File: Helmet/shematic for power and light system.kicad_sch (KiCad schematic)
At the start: 10 parts, among them Q1 IRLZ44N, SW1 SW_DIP_x01, U1 LM340K-5.0/NOPB, U2 LP2950-3.3_TO252, U3 ESP32-WROOM-32, U4 LM340K-5.0/NOPB, U5 ESP32-WROOM-32, U6 LP2950-3.3_TO252

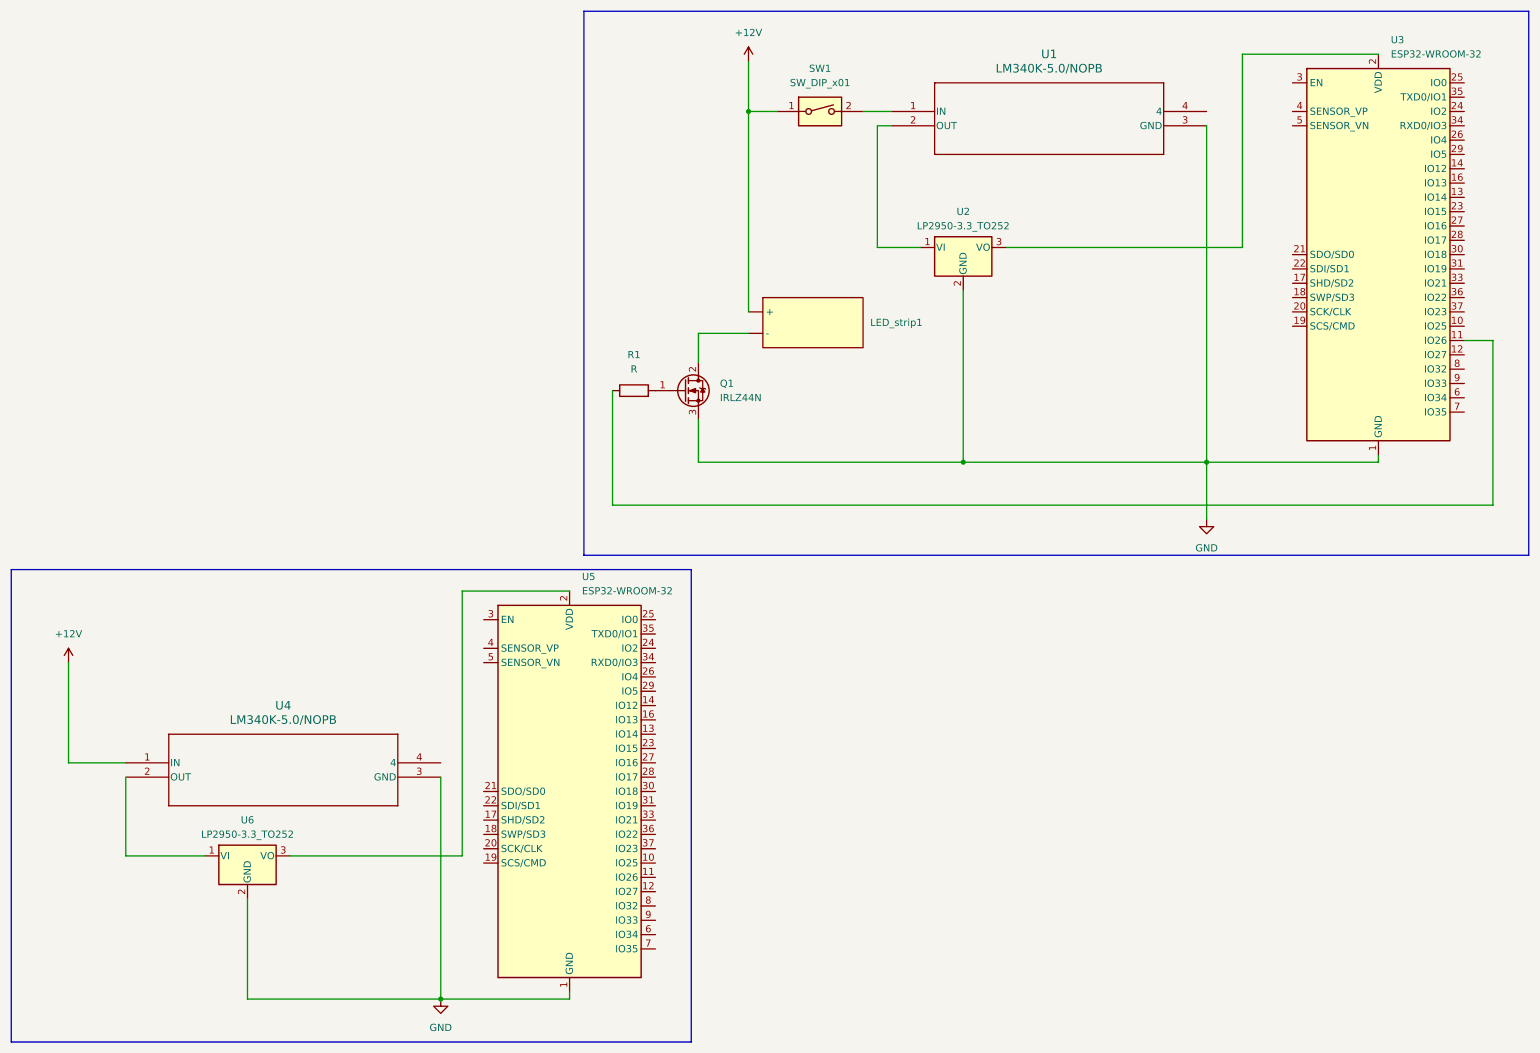
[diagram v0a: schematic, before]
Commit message: adding inital pcb schematics
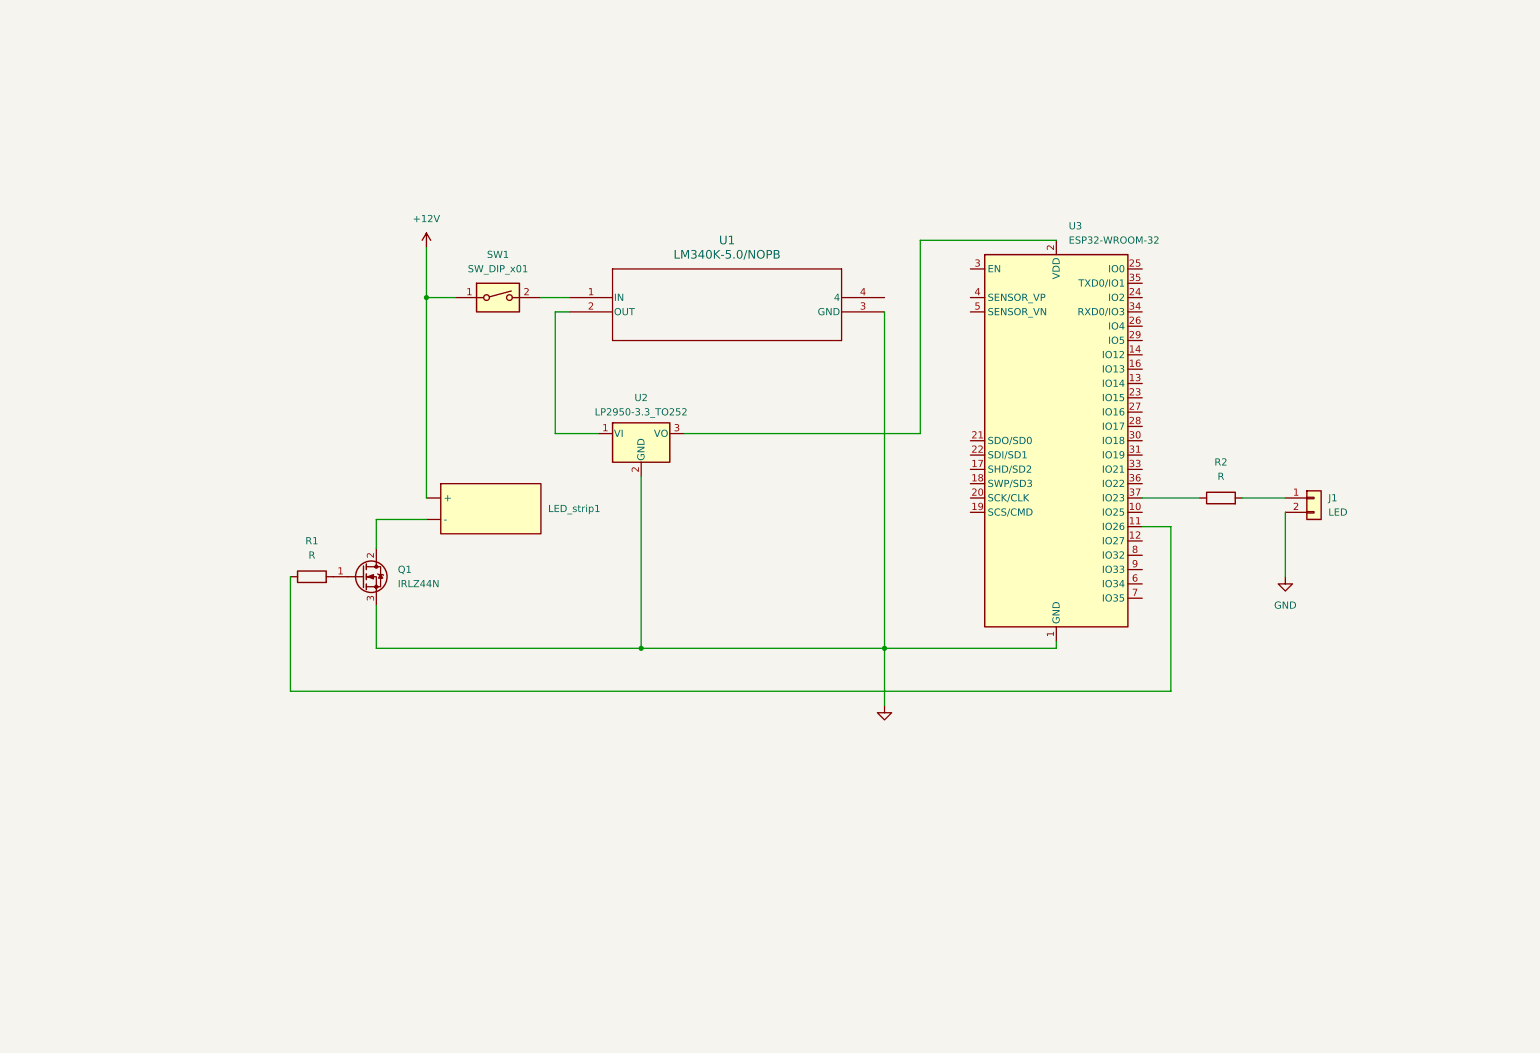
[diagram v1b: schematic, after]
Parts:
- removed U4: LM340K-5.0/NOPB, K02A_TEX, symbol LM340K_5:LM340K-5.0_NOPB
- removed U5: ESP32-WROOM-32, RF_Module:ESP32-WROOM-32, symbol RF_Module:ESP32-WROOM-32
- removed U6: LP2950-3.3_TO252, Package_TO_SOT_SMD:TO-252-2, symbol Regulator_Linear:LP2950-3.3_TO252
- added J1: LED, symbol Connector_Generic:Conn_01x02
- added R2: R, symbol Device:R
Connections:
- net GND: now also J1.2 (Pin_2)
- net at U3.37 (IO23): now also R2.1
- new net: J1.1 (Pin_1), R2.2
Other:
- moved on the sheet: LED_strip1, Q1, R1, SW1, U1, U2, U3

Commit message: first draft PCB done
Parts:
- J1, LED_strip1: footprint (none) -> Connector_Molex:Molex_KK-254_AE-6410-02A_1x02_P2.54mm_Vertical
- R1, R2: footprint (none) -> Resistor_SMD:R_0805_2012Metric_Pad1.20x1.40mm_HandSolder
- SW1: footprint (none) -> Button_Switch_THT:SW_DIP_SPSTx01_Slide_9.78x4.72mm_W7.62mm_P2.54mm
- U1: footprint K02A_TEX -> footprints:LM340K-5.0&slash_NOPB
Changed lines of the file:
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@@
       (effects (font (size 1.27 1.27)))
     )
-    (property "Footprint" "" (at 97.79 95.25 0)
+    (property "Footprint" "Connector_Molex:Molex_KK-254_AE-6410-02A_1x02_P2.54mm_Vertical" (at 97.79 95.25 0)
       (effects (font (size 1.27 1.27)) hide)
     )
@@
       (effects (font (size 1.27 1.27)))
     )
-    (property "Footprint" "" (at 66.04 116.078 90)
+    (property "Footprint" "Resistor_SMD:R_0805_2012Metric_Pad1.20x1.40mm_HandSolder" (at 66.04 116.078 90)
       (effects (font (size 1.27 1.27)) hide)
     )
@@
       (effects (font (size 1.524 1.524)))
     )
-    (property "Footprint" "K02A_TEX" (at 111.76 64.77 0)
+    (property "Footprint" "footprints:LM340K-5.0&slash_NOPB" (at 111.76 64.77 0)
       (effects (font (size 1.27 1.27) italic) hide)
     )
@@
       (effects (font (size 1.27 1.27)))
     )
-    (property "Footprint" "" (at 99.06 64.77 0)
+    (property "Footprint" "Button_Switch_THT:SW_DIP_SPSTx01_Slide_9.78x4.72mm_W7.62mm_P2.54mm" (at 99.06 64.77 0)
       (effects (font (size 1.27 1.27)) hide)
     )
@@
       (effects (font (size 1.27 1.27)) (justify left))
     )
-    (property "Footprint" "" (at 243.84 100.33 0)
+    (property "Footprint" "Connector_Molex:Molex_KK-254_AE-6410-02A_1x02_P2.54mm_Vertical" (at 243.84 100.33 0)
       (effects (font (size 1.27 1.27)) hide)
     )
@@
       (effects (font (size 1.27 1.27)))
     )
-    (property "Footprint" "" (at 227.33 102.108 90)
-      (effects (font (size 1.27 1.27)) hide)
-    )
+    (property "Footprint" "Resistor_SMD:R_0805_2012Metric_Pad1.20x1.40mm_HandSolder" (at 227.33 102.108 90)
+      (effects (font (size 1.27 1.27)) hide)
+    )
